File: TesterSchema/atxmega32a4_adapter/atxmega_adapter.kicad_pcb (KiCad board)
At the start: 2 copper layers, 55 x 20 mm, 23 parts, among them IC1 ATXMEGA32A4-M, P1 DIL40, Q1 BC817-40, Q2 BC817-40, Q3 BC817-40

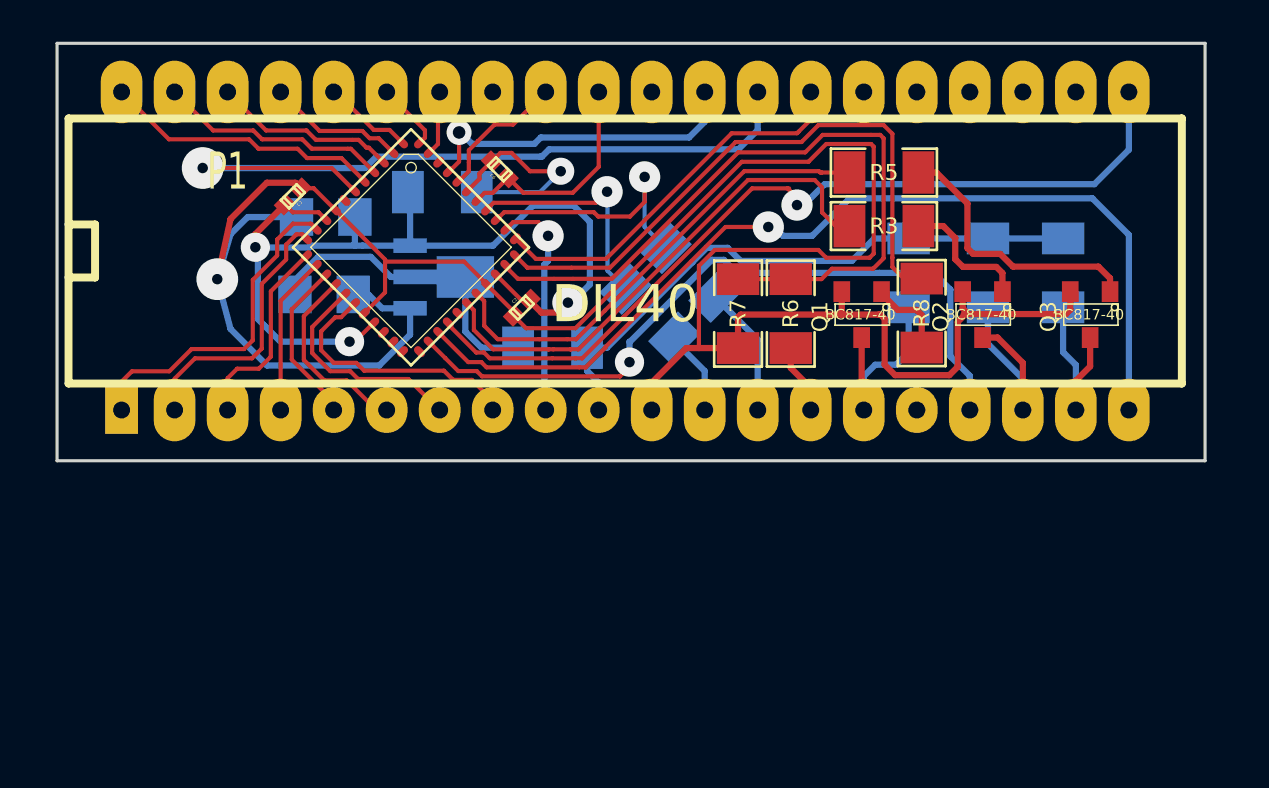
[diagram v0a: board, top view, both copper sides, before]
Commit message: Zmiany w projekcie przejściówki (wykorzystanie elementów dostępnych w standardowych bibliotekach + zmiana footprintu atmego bo był zły :/ )
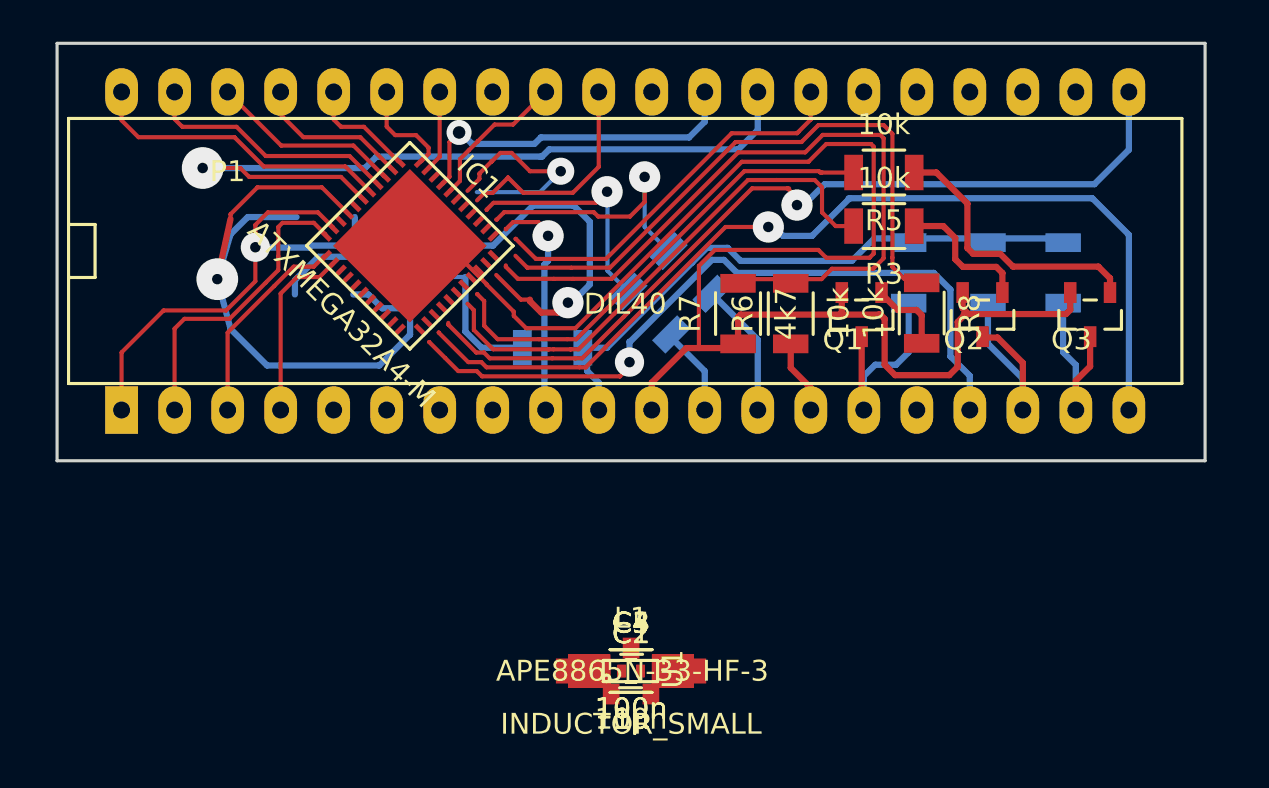
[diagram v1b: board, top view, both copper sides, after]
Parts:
- removed C6: 100n, c_0402
- removed US1: APE8800-3, sot89
- added C3: 1µ, Capacitors_SMD:C_1206_HandSoldering, F.Cu at (236.5, 128.1)
- added U1: APE8865N-33-HF-3, SMD_Packages:SOT-23, F.Cu at (236.5, 128.1)
- C1, C2: footprint c_0402 -> Resistors_SMD:R_0402
- C4: footprint c_1206 -> Capacitors_SMD:C_1206_HandSoldering; moved to F.Cu
- C5: value 1µ -> 100n; footprint c_1206 -> Capacitors_SMD:C_1206_HandSoldering; moved to F.Cu
- IC1: footprint microchip-dspic-QFN44-8X8 -> SMD_Packages:QFN-44-1EP
- L1: value L -> INDUCTOR_SMALL; footprint SM1206 -> Choke_SMD:Choke_SMD_1206_Handsoldering; moved to F.Cu
- P1: footprint DIP-40__600_ELL -> Sockets_DIP:DIP-40__600_ELL
- Q1, Q2, Q3: footprint SOT23 -> Transistors_SMD:sot23
- R1, R10, R11, R2, R3, R4, R5, R6, R7, R8, R9: footprint SM1206 -> Resistors_SMD:R_1206
- moved C1 27.9 mm to (236.5, 128.1), turned to 0 degrees
- moved C5 26.2 mm to (236.5, 128.1)
- moved L1 24.7 mm to (236.5, 128.1), turned to 0 degrees
- moved C4 23.3 mm to (236.5, 128.1), turned to 0 degrees
- moved C2 18.2 mm to (236.5, 128.1), turned to 0 degrees
- moved IC1 0.09 mm to (225.9, 107.7), turned to 315 degrees
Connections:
- C4 pad 1: N-0000028 -> +3.3V
- C5 pad 1: +3.3V -> +3.3VADC
- C5 pad 2: GND -> AGND
- L1 pad 1: +3.3VADC -> +3.3V
- L1 pad 2: +3.3V -> +3.3VADC
- R11 pad 2: N-0000028 -> Net-(C3-Pad1)
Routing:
- net +3.3V: track 45.2 -> 0.00 mm, vias 3 -> 0
- net /DB0: track 16.1 -> 48.6 mm, vias 0 -> 2
- net Net-(IC1-Pad33): track 29.3 -> 47.7 mm
- net Net-(IC1-Pad32): track 34.5 -> 16.1 mm
- net N-0000028: track 15.2 -> 0.00 mm
- net Net-(C3-Pad1): track 0.00 -> 15.2 mm
- net /DB7: track 12.7 -> 0.45 mm
- net /RESET: track 11.1 -> 22.4 mm, vias 1 -> 2
- net /XTAL2: track 12.7 -> 1.42 mm, vias 1 -> 0
- net /DB6: track 10.7 -> 0.01 mm
- net /DB5: track 9.20 -> 0.50 mm
- net /DB4: track 7.98 -> 0.41 mm
- net AGND: track 10.7 -> 5.34 mm
- net /XTAL1: track 11.2 -> 16.5 mm
- net GND: track 116.7 -> 112.5 mm
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
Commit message: Poprawa schematu płytki
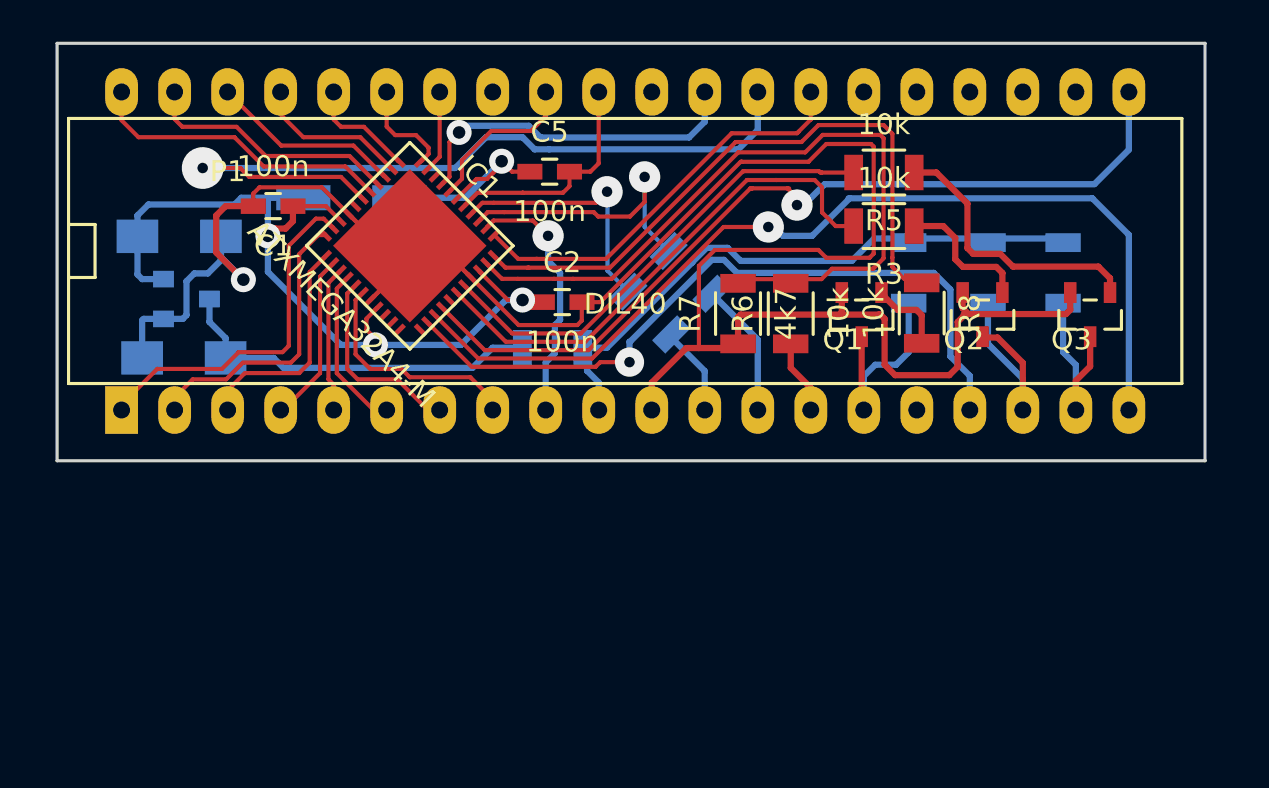
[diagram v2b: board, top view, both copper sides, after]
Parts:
- C1, C2: footprint Resistors_SMD:R_0402 -> Capacitors_SMD:C_0603_HandSoldering
- C3, C4, L1, U1: moved to B.Cu
- C5: footprint Capacitors_SMD:C_1206_HandSoldering -> Capacitors_SMD:C_0603_HandSoldering
- moved C4 30.0 mm to (214.8, 107.2)
- moved C1 28.1 mm to (219.3, 105.8), turned to 180 degrees
- moved U1 27.8 mm to (215.2, 110.2), turned to 90 degrees
- moved L1 26.3 mm to (223.1, 105.4)
- moved C3 26.2 mm to (215.1, 113.1), turned to 180 degrees
- moved C5 24.2 mm to (232.6, 104.2)
- moved C2 18.0 mm to (233.2, 110.4)
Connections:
- IC1 pad 45: (no net) -> GND
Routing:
- net +3.3V: track 0.00 -> 41.2 mm, vias 0 -> 3
- net /DB0: track 48.6 -> 17.1 mm, vias 2 -> 0
- net Net-(IC1-Pad32): track 16.1 -> 35.4 mm
- net Net-(IC1-Pad33): track 47.7 -> 30.4 mm
- net /XTAL2: track 1.42 -> 13.5 mm, vias 0 -> 1
- net /DB7: track 0.45 -> 11.5 mm
- net /RESET: track 22.4 -> 12.5 mm, vias 2 -> 1
- net /DB6: track 0.01 -> 9.38 mm
- net /DB5: track 0.50 -> 8.37 mm
- net GND: track 112.5 -> 120.4 mm
- net /DB4: track 0.41 -> 6.99 mm
- net AGND: track 5.34 -> 11.1 mm
- net /XTAL1: track 16.5 -> 11.9 mm
- net Net-(C3-Pad1): track 15.2 -> 18.2 mm
- net /PDI_DATA: track 18.6 -> 19.8 mm
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
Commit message: poprawki płytki
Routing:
- net +3.3V: track 41.2 -> 45.7 mm
- net GND: track 120.4 -> 116.8 mm
- net /SW1: track 38.2 -> 36.8 mm
- net /DB5: track 8.37 -> 7.05 mm
- net Net-(Q3-Pad1): track 13.2 -> 11.9 mm
- net /DB7: track 11.5 -> 10.3 mm
- net Net-(IC1-Pad32): track 35.4 -> 36.5 mm
- net /RESET: track 12.5 -> 13.4 mm
- net Net-(IC1-Pad28): track 24.6 -> 23.7 mm
- net /ADC_I: track 5.39 -> 4.73 mm
- net /E: track 7.48 -> 6.85 mm
- net Net-(Q2-Pad1): track 6.45 -> 5.85 mm
- net /ADC_U: track 14.6 -> 14.1 mm
- net /DB6: track 9.38 -> 8.83 mm
- net /RS: track 12.3 -> 11.7 mm

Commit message: zmiany z adapterze
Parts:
- moved L1 1.57 mm to (223.4, 103.8)
- moved C2 1.09 mm to (232.1, 110.2), turned to 180 degrees
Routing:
- net +3.3V: track 45.7 -> 54.0 mm
- net /RESET: track 13.4 -> 18.1 mm
- net /XTAL1: track 11.9 -> 15.7 mm
- net /PDI_DATA: track 19.6 -> 18.2 mm
- net Net-(IC1-Pad32): track 36.5 -> 35.1 mm
- net Net-(IC1-Pad33): track 30.4 -> 29.0 mm
- net /DB2: track 10.8 -> 9.45 mm
- net GND: track 116.8 -> 118.0 mm
- net /DB1: track 13.9 -> 12.7 mm
- net /OW: track 16.7 -> 15.6 mm
- net +3.3VADC: track 10.5 -> 9.56 mm
- net /DB0: track 17.1 -> 16.2 mm
- net /XTAL2: track 13.4 -> 14.1 mm
- net /DB7: track 10.3 -> 9.71 mm
- net /DB6: track 8.83 -> 8.21 mm
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
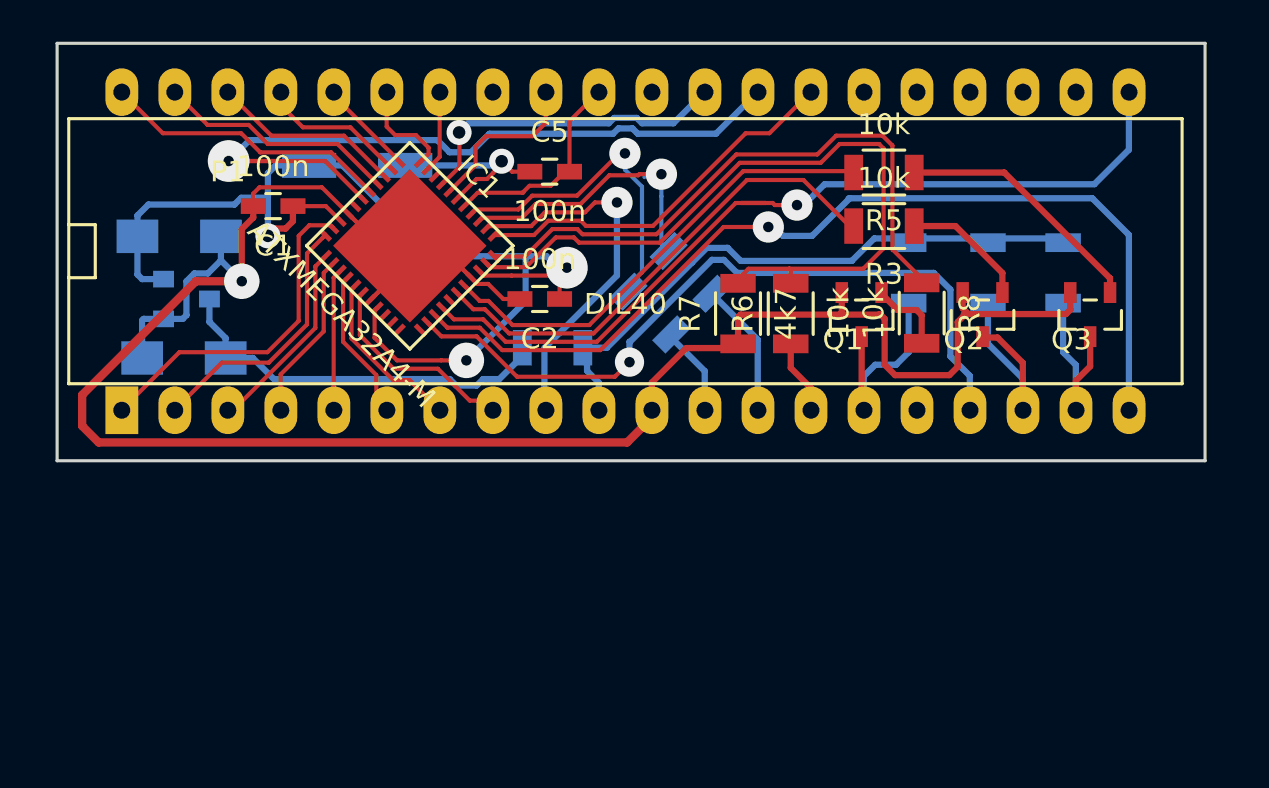
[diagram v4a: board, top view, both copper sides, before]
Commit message: Dodanie diody sygnalizującej zasilanie i 2 diodek pomocniczych
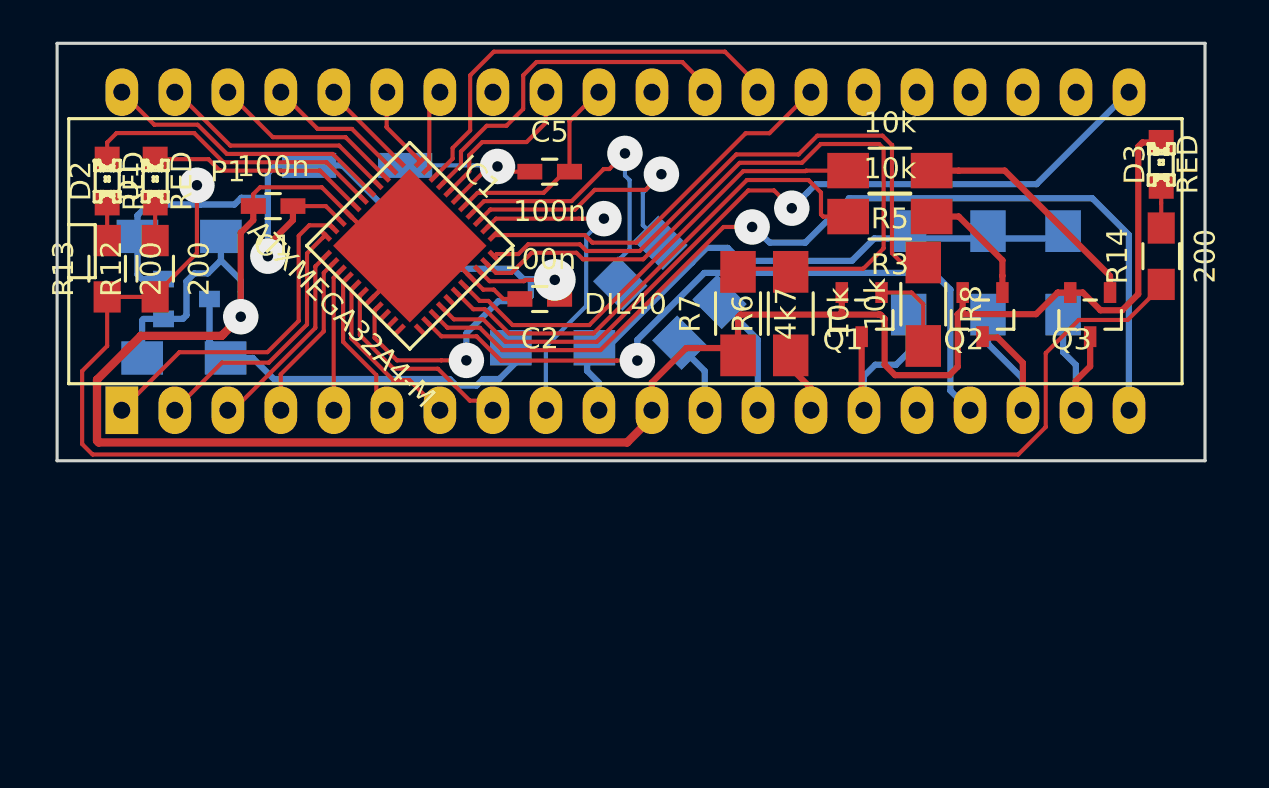
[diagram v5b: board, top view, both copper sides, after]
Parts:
- added D1: RED, LEDs:LED-0805, F.Cu at (213.7, 104.6)
- added D2: RED, LEDs:LED-0805, F.Cu at (211.4, 104.6)
- added D3: RED, LEDs:LED-0805, F.Cu at (261.9, 103.8)
- added R12: 200, Resistors_SMD:R_0805_HandSoldering, F.Cu at (213.7, 108.8)
- added R13: 200, Resistors_SMD:R_0805_HandSoldering, F.Cu at (211.4, 108.8)
- added R14: 200, Resistors_SMD:R_0805_HandSoldering, F.Cu at (261.9, 108.2)
- R1, R10, R11, R2, R3, R4, R5, R6, R7, R8, R9: footprint Resistors_SMD:R_1206 -> Resistors_SMD:R_1206_HandSoldering
- moved R3 0.54 mm to (248.9, 106.3)
- moved R8 0.43 mm to (250.5, 110.5)
- moved R5 0.30 mm to (248.9, 104.1)
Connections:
- IC1 pad 42: (no net) -> /SW1
- IC1 pad 45: GND -> (no net)
- IC1 pad 6: /SW1 -> Net-(D2-Pad2)
- IC1 pad 7: (no net) -> Net-(D1-Pad2)
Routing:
- net +3.3V: track 54.0 -> 129.4 mm, vias 3 -> 4
- net /SW1: track 36.9 -> 20.8 mm, vias 1 -> 0
- net Net-(D2-Pad2): track 0.00 -> 14.5 mm
- net Net-(D1-Pad2): track 0.00 -> 10.5 mm
- net GND: track 118.0 -> 126.4 mm
- net (no net): track 0.00 -> 5.36 mm
- net /SW4: track 41.4 -> 39.2 mm
- net Net-(D3-Pad1): track 0.00 -> 2.00 mm
- net Net-(D2-Pad1): track 0.00 -> 1.80 mm
- net Net-(D1-Pad1): track 0.00 -> 1.80 mm
- net /RESET: track 18.1 -> 16.4 mm
- net /OW: track 15.6 -> 17.1 mm, vias 1 -> 0
- net /NO_ADC: track 4.92 -> 3.99 mm
- net +3.3VADC: track 9.56 -> 8.65 mm
- net /XTAL1: track 15.7 -> 15.0 mm

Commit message: Dodany program testowy, oraz małe poprawki w płytce adaptera
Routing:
- net GND: track 126.4 -> 129.2 mm
- net +3.3V: track 129.4 -> 131.7 mm
- net /PWM_CHG: track 8.93 -> 9.44 mm

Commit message: Zmiana kilku pierdół
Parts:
- moved C2 0.53 mm to (232.4, 110.7)
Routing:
- net +3.3V: track 131.7 -> 132.3 mm

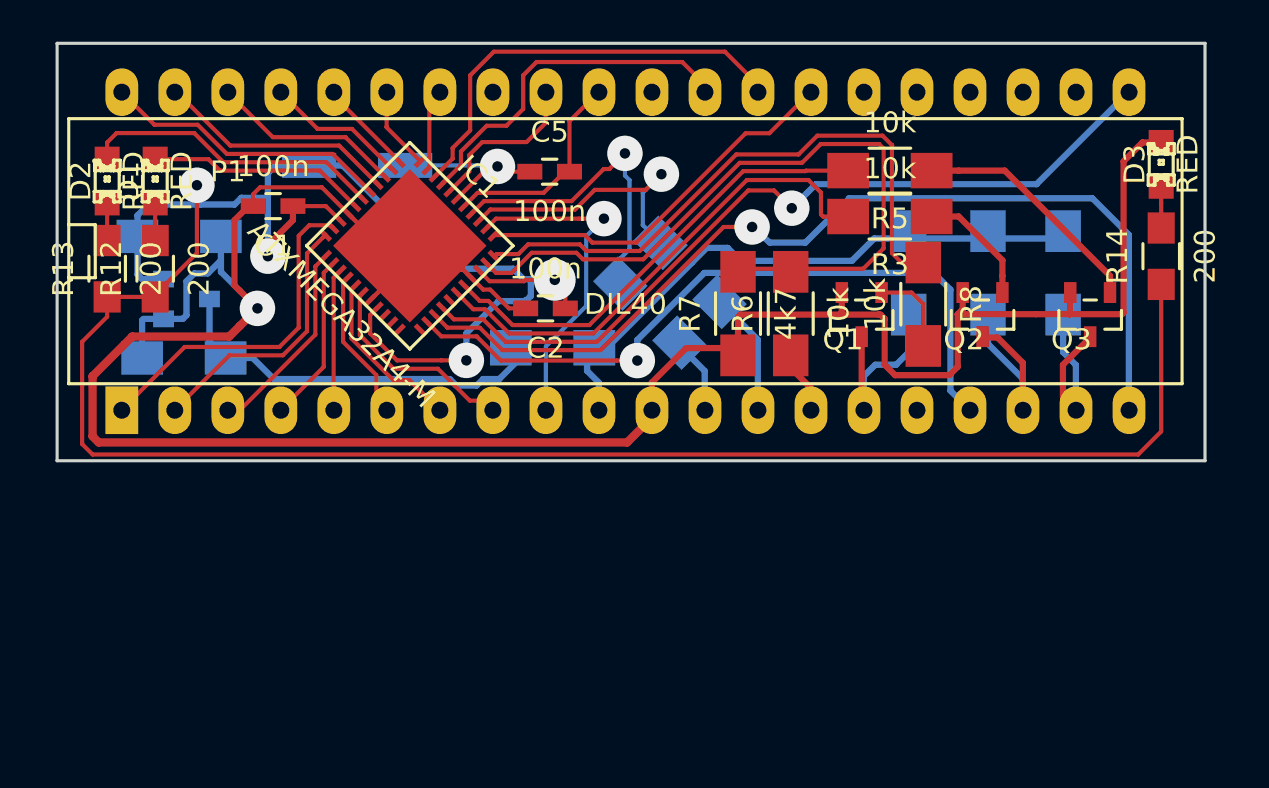
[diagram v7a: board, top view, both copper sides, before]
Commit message: poprawienie płytki
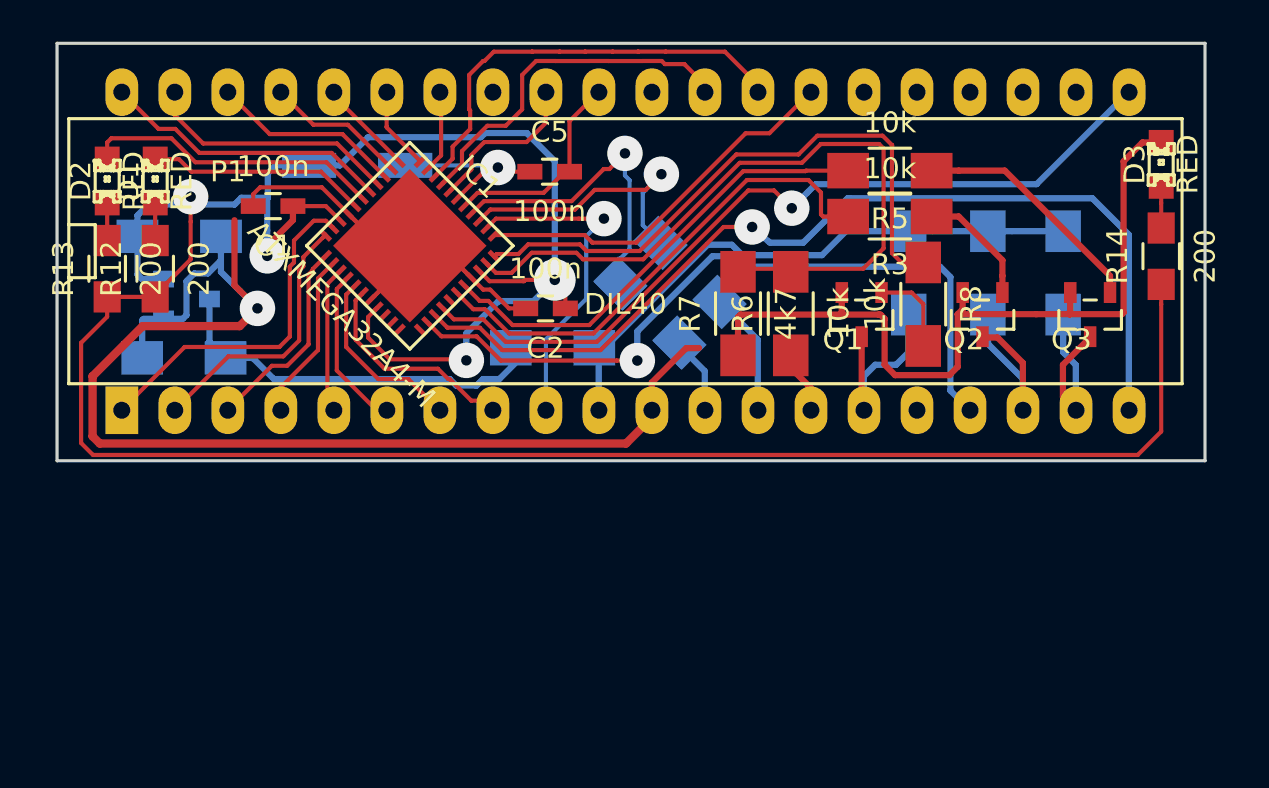
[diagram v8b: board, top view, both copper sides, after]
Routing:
- net +3.3V: track 132.3 -> 135.7 mm
- net GND: track 128.9 -> 126.1 mm
- net /SW2: track 35.5 -> 36.8 mm
- net VCC: track 28.7 -> 27.8 mm
- net /RS: track 11.5 -> 12.2 mm
- net /DB6: track 8.21 -> 8.81 mm
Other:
- net class Default: clearance 0.2 -> 0.25
- rule trace_clearance: 0.2 -> 0.25
